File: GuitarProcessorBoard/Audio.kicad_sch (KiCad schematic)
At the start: 33 parts, among them U201 TLV320AIC3204, U202 TL074

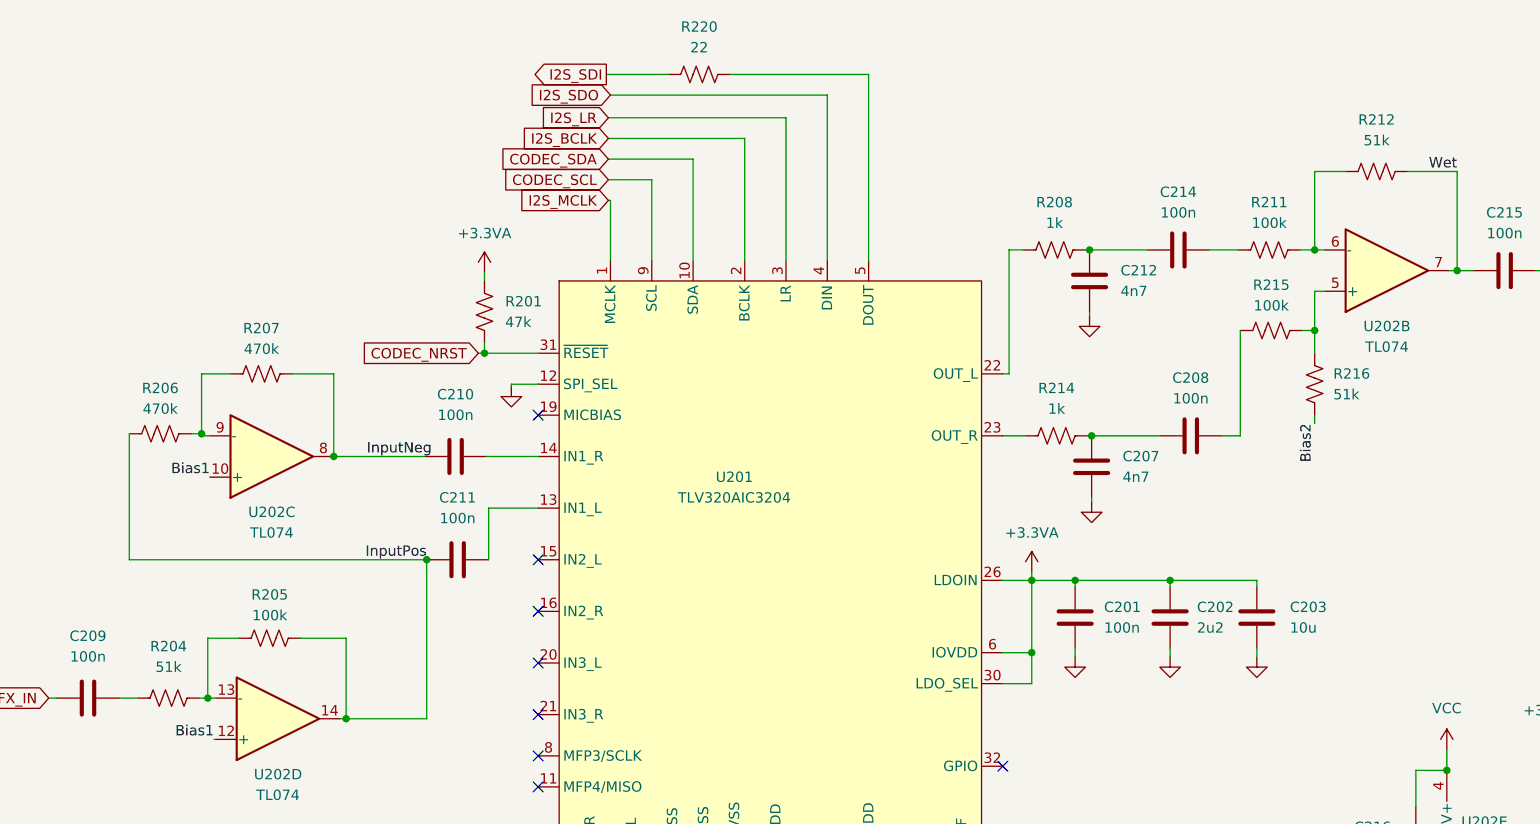
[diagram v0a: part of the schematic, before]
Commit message: tweaked resistor for input/output gain
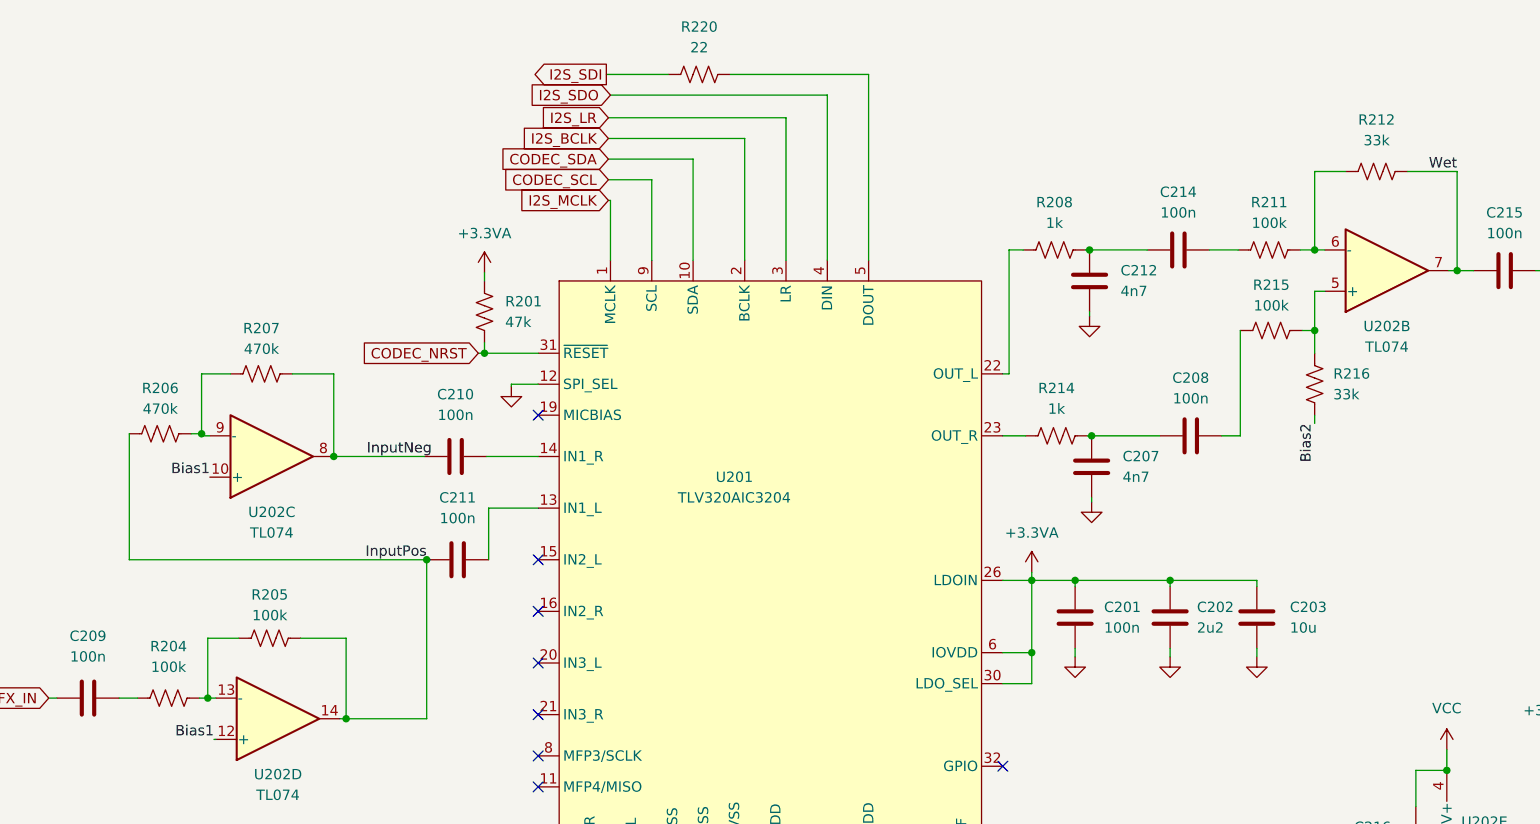
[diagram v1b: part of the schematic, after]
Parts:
- R204: value 51k -> 100k
- R212, R216: value 51k -> 33k
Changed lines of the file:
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@@
 			)
 		)
-		(property "Value" "51k"
+		(property "Value" "100k"
 			(at 38.354 107.95 90)
 			(effects
@@
 			)
 		)
-		(property "Value" "51k"
+		(property "Value" "33k"
 			(at 186.944 43.18 90)
 			(effects
@@
 			)
 		)
-		(property "Value" "51k"
+		(property "Value" "33k"
 			(at 181.61 74.4219 0)
 			(effects

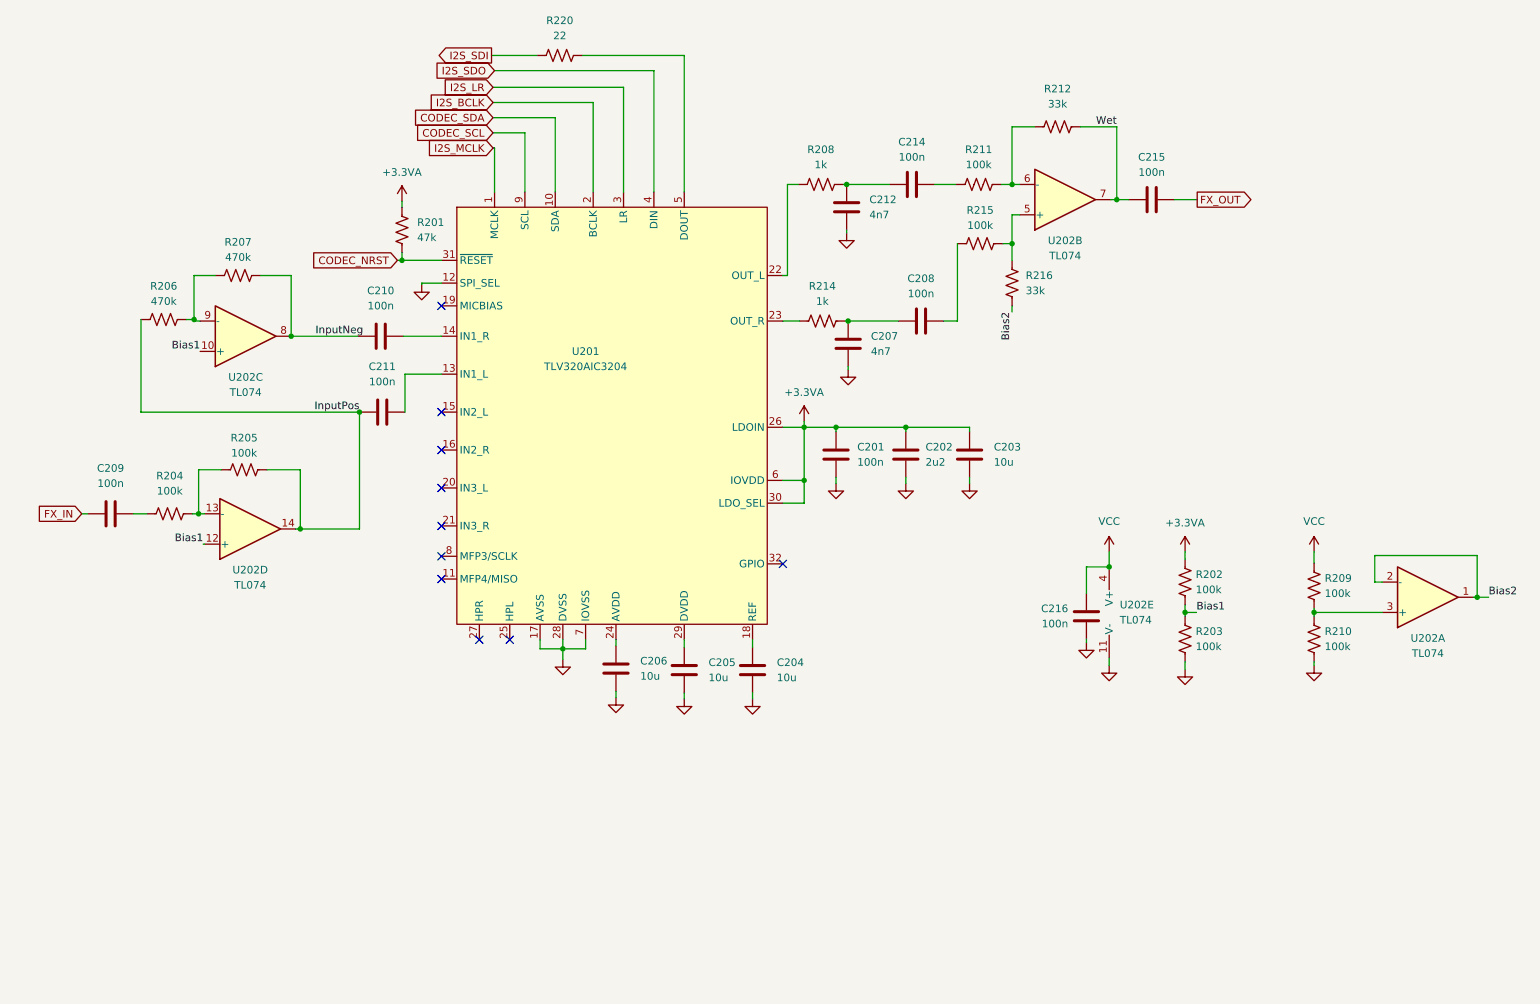
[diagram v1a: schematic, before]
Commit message: updated schematic, re-annotated
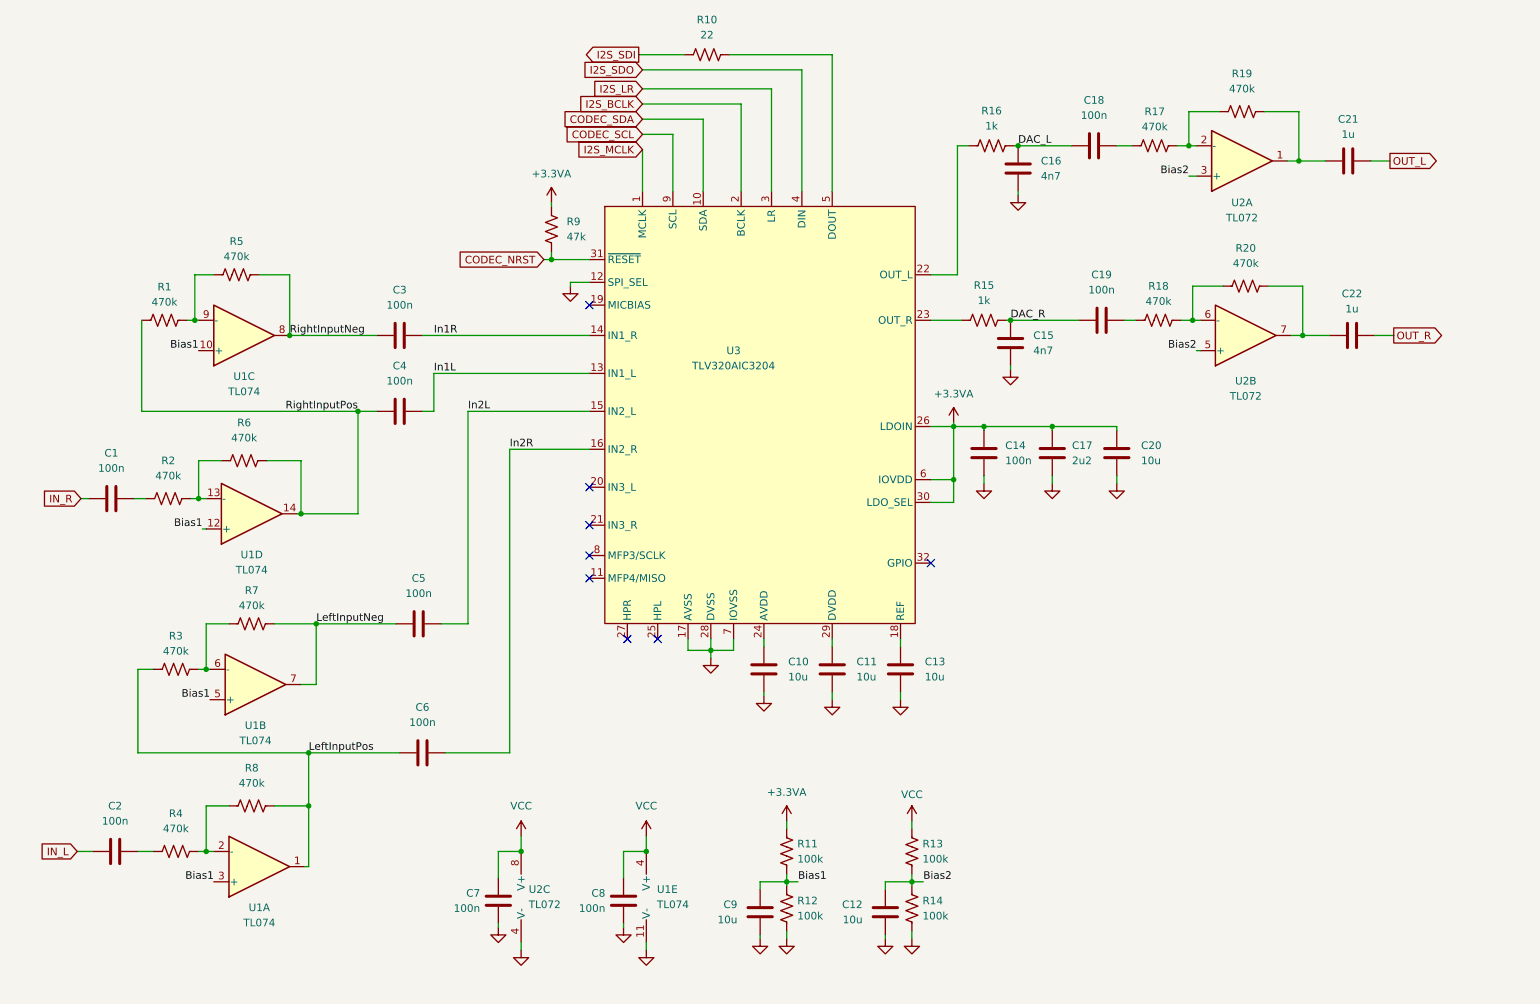
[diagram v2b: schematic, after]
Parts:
- removed C208, C214, C215: 100n, Capacitor_SMD:C_0805_2012Metric, symbol Device:C
- removed R209, R210, R211, R215: 100k, Resistor_SMD:R_0805_2012Metric, symbol Device:R_US
- removed R212, R216: 33k, Resistor_SMD:R_0805_2012Metric, symbol Device:R_US
- added C12, C9: 10u, Capacitor_SMD:C_0805_2012Metric, symbol Device:C
- added C18, C19, C2, C5, C6, C7: 100n, Capacitor_SMD:C_0805_2012Metric, symbol Device:C
- added C21, C22: 1u, Capacitor_SMD:C_0805_2012Metric, symbol Device:C
- added R13, R14: 100k, Resistor_SMD:R_0805_2012Metric, symbol Device:R_US
- added R17, R18, R19, R20, R3, R4, R7, R8: 470k, Resistor_SMD:R_0805_2012Metric, symbol Device:R_US
- added U2: TL072, Package_SO:SOIC-8_3.9x4.9mm_P1.27mm, symbol Amplifier_Operational:TL072
- R2: renamed from R204; value 100k -> 470k
- R6: renamed from R205; value 100k -> 470k
- renumbered C209 to C1, C206 to C10, C205 to C11, C204 to C13, C201 to C14, C207 to C15, C212 to C16, C202 to C17, C203 to C20, C210 to C3, C211 to C4, C216 to C8, R206 to R1, R220 to R10, R202 to R11, R203 to R12, R214 to R15, R208 to R16, R207 to R5, R201 to R9, U202 to U1, U201 to U3
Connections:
- net Bias1: now also U1.3 (+), U1.5 (+), C9.1
- net Bias2: now also C12.1, R13.2, R14.1, U2.3 (+), U2.5 (+); no longer U1.1, U1.2 (-)
- net GND: now also C12.2, C7.2, C9.2, R14.2, U2.4 (V-)
- net VCC: now also C7.1, R13.1, U2.8 (V+)
- net DAC_L: now reaches C16.1, R16.2
- net DAC_L: now also C18.1
- net In1L: now reaches C4.2, U3.13 (IN1_L)
- net In1R: now reaches C3.2, U3.14 (IN1_R)
- net In2L: now reaches U3.15 (IN2_L)
- net In2L: now also C5.2
- net In2R: now reaches U3.16 (IN2_R)
- net In2R: now also C6.2
- net DAC_R: now reaches C15.1, R15.2
- net DAC_R: now also C19.1
- net at U1.6 (-): now also R3.2, R7.1
- net FX_IN renamed IN_R
- net InputNeg renamed RightInputNeg
- net InputPos renamed RightInputPos
- net Wet renamed LeftInputNeg
- net LeftInputNeg: now also C5.1, R7.2
- new net: C22.1, R20.2, U2.7
- new net: R4.2, R8.1, U1.2 (-)
- new net: C2.2, R4.1
- new net: C19.2, R18.1
- new net: R18.2, R20.1, U2.6 (-)
- new net: C21.1, R19.2, U2.1
- new net: R17.2, R19.1, U2.2 (-)
- new net: C18.2, R17.1
- new net IN_L: C2.1
- new net LeftInputPos: C6.1, R3.1, R8.2, U1.1
- new net OUT_L: C21.2
- new net OUT_R: C22.2
- no-connect marks 10 -> 8
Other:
- moved on the sheet: C1, C10, C11, C13, C14, C15, C16, C17, C20, C3, C4, C8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

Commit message: new layout
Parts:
- added TP10: DACR, TestPoint:TestPoint_THTPad_D2.0mm_Drill1.0mm_VAL, symbol Connector:TestPoint
- added TP9: DACL, TestPoint:TestPoint_THTPad_D2.0mm_Drill1.0mm_VAL, symbol Connector:TestPoint
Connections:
- net DAC_L: now also TP9.1
- net DAC_R: now also TP10.1
- net LeftInputNeg: now also U1.8; no longer U1.7
- net LeftInputPos: now also U1.7; no longer U1.1
- net RightInputNeg: now also U1.14; no longer U1.8
- net RightInputPos: now also U1.1; no longer U1.14
- net at R3.2, R7.1: now also U1.9 (-); no longer U1.6 (-)
- net at R1.2, R5.1: now also U1.13 (-); no longer U1.9 (-)
- net at C22.1, R20.2: now also U2.1; no longer U2.7
- net at R4.2, R8.1: now also U1.6 (-); no longer U1.2 (-)
- net at R2.2, R6.1: now also U1.2 (-); no longer U1.13 (-)
- net at R18.2, R20.1: now also U2.2 (-); no longer U2.6 (-)
- net at C21.1, R19.2: now also U2.7; no longer U2.1
- net at R17.2, R19.1: now also U2.6 (-); no longer U2.2 (-)
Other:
- moved on the sheet: U1A, U1B, U1C, U1D, U2A, U2B

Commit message: prelim. routing, DRC passing
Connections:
- net +3.3VA: no longer R9.1
- net LeftInputNeg: now also R7.1; no longer R7.2
- net at R3.2, U1.9 (-): now also R7.2; no longer R7.1
- new net +3.3V: R9.1
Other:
- moved on the sheet: R7
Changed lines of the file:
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@@
 	(symbol
 		(lib_id "Device:R_US")
-		(at 52.07 130.175 90)
-		(unit 1)
-		(body_style 1)
-		(exclude_from_sim no)
-		(in_bom yes)
-		(on_board yes)
-		(in_pos_files yes)
-		(dnp no)
-		(fields_autoplaced yes)
+		(at 52.07 130.175 270)
+		(mirror x)
+		(unit 1)
+		(body_style 1)
+		(exclude_from_sim no)
+		(in_bom yes)
+		(on_board yes)
+		(in_pos_files yes)
+		(dnp no)
 		(property "Reference" "R7"
 			(at 52.07 124.587 90)
@@
 		)
 		(property "Footprint" "Resistor_SMD:R_0805_2012Metric"
-			(at 52.324 129.159 90)
+			(at 51.816 129.159 90)
 			(hide yes)
 			(show_name no)
@@
 				(path "/524c695b-c632-4089-9e9a-ef0f89cad1b2/ef3a9a4a-abe1-4d77-855c-3594c7f88930"
 					(reference "R13")
-					(unit 1)
-				)
-			)
-		)
-	)
-	(symbol
-		(lib_id "power:+3.3VA")
-		(at 102.235 59.69 0)
-		(unit 1)
-		(body_style 1)
-		(exclude_from_sim no)
-		(in_bom yes)
-		(on_board yes)
-		(in_pos_files yes)
-		(dnp no)
-		(fields_autoplaced yes)
-		(property "Reference" "#PWR04"
-			(at 102.235 63.5 0)
-			(hide yes)
-			(show_name no)
-			(do_not_autoplace no)
-			(effects
-				(font
-					(size 1.27 1.27)
-				)
-			)
-		)
-		(property "Value" "+3.3VA"
-			(at 102.235 54.864 0)
-			(show_name no)
-			(do_not_autoplace no)
-			(effects
-				(font
-					(size 1.27 1.27)
-				)
-			)
-		)
-		(property "Footprint" ""
-			(at 102.235 59.69 0)
-			(hide yes)
-			(show_name no)
-			(do_not_autoplace no)
-			(effects
-				(font
-					(size 1.27 1.27)
-				)
-			)
-		)
-		(property "Datasheet" ""
-			(at 102.235 59.69 0)
-			(hide yes)
-			(show_name no)
-			(do_not_autoplace no)
-			(effects
-				(font
-					(size 1.27 1.27)
-				)
-			)
-		)
-		(property "Description" "Power symbol creates a global label with name \"+3.3VA\""
-			(at 102.235 59.69 0)
-			(hide yes)
-			(show_name no)
-			(do_not_autoplace no)
-			(effects
-				(font
-					(size 1.27 1.27)
-				)
-			)
-		)
-		(pin "1"
-		)
-		(instances
-			(project "GuitarProcessorBoard"
-				(path "/524c695b-c632-4089-9e9a-ef0f89cad1b2/ef3a9a4a-abe1-4d77-855c-3594c7f88930"
-					(reference "#PWR04")
 					(unit 1)
 				)
@@
 					(unit 1)
 				)
+			)
+		)
+	)
+	(symbol
+		(lib_id "power:+3.3V")
+		(at 102.235 59.69 0)
+		(unit 1)
+		(body_style 1)
+		(exclude_from_sim no)
+		(in_bom yes)
+		(on_board yes)
+		(in_pos_files yes)
+		(dnp no)
+		(fields_autoplaced yes)
+		(property "Reference" "#PWR04"
+			(at 102.235 63.5 0)
+			(hide yes)
+			(show_name no)
+			(do_not_autoplace no)
+			(effects
+				(font
+					(size 1.27 1.27)
+				)
+			)
+		)
+		(property "Value" "+3.3V"
+			(at 102.235 54.61 0)
+			(show_name no)
+			(do_not_autoplace no)
+			(effects
+				(font
+					(size 1.27 1.27)
+				)
+			)
+		)
+		(property "Footprint" ""
+			(at 102.235 59.69 0)
+			(hide yes)
+			(show_name no)
+			(do_not_autoplace no)
+			(effects
+				(font
+					(size 1.27 1.27)
+				)
+			)
+		)
+		(property "Datasheet" ""
+			(at 102.235 59.69 0)
+			(hide yes)
+			(show_name no)
+			(do_not_autoplace no)
+			(effects
+				(font
+					(size 1.27 1.27)
+				)
+			)
+		)
+		(property "Description" "Power symbol creates a global label with name \"+3.3V\""
+			(at 102.235 59.69 0)
+			(hide yes)
+			(show_name no)
+			(do_not_autoplace no)
+			(effects
+				(font
+					(size 1.27 1.27)
+				)
+			)
+		)
+		(pin "1"
+		)
+		(instances
+			(project "GuitarProcessorBoard"
+				(path "/524c695b-c632-4089-9e9a-ef0f89cad1b2/ef3a9a4a-abe1-4d77-855c-3594c7f88930"
+					(reference "#PWR04")
+					(unit 1)
+				)

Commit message: new layout, pinout switcharoo
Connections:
- net +3.3V is gone; now on net +3.3VA: R9.1
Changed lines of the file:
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@@
-	)
-	(symbol
-		(lib_id "power:+3.3V")
-		(at 102.235 59.69 0)
-		(unit 1)
-		(body_style 1)
-		(exclude_from_sim no)
-		(in_bom yes)
-		(on_board yes)
-		(in_pos_files yes)
-		(dnp no)
-		(fields_autoplaced yes)
-		(property "Reference" "#PWR04"
-			(at 102.235 63.5 0)
-			(hide yes)
-			(show_name no)
-			(do_not_autoplace no)
-			(effects
-				(font
-					(size 1.27 1.27)
-				)
-			)
-		)
-		(property "Value" "+3.3V"
-			(at 102.235 54.61 0)
-			(show_name no)
-			(do_not_autoplace no)
-			(effects
-				(font
-					(size 1.27 1.27)
-				)
-			)
-		)
-		(property "Footprint" ""
-			(at 102.235 59.69 0)
-			(hide yes)
-			(show_name no)
-			(do_not_autoplace no)
-			(effects
-				(font
-					(size 1.27 1.27)
-				)
-			)
-		)
-		(property "Datasheet" ""
-			(at 102.235 59.69 0)
-			(hide yes)
-			(show_name no)
-			(do_not_autoplace no)
-			(effects
-				(font
-					(size 1.27 1.27)
-				)
-			)
-		)
-		(property "Description" "Power symbol creates a global label with name \"+3.3V\""
-			(at 102.235 59.69 0)
-			(hide yes)
-			(show_name no)
-			(do_not_autoplace no)
-			(effects
-				(font
-					(size 1.27 1.27)
-				)
-			)
-		)
-		(pin "1"
-		)
-		(instances
-			(project "GuitarProcessorBoard"
-				(path "/524c695b-c632-4089-9e9a-ef0f89cad1b2/ef3a9a4a-abe1-4d77-855c-3594c7f88930"
-					(reference "#PWR04")
-					(unit 1)
-				)
-			)
-		)
 	)
 	(symbol
@@
 					(unit 1)
 				)
+			)
+		)
+	)
+	(symbol
+		(lib_id "power:+3.3VA")
+		(at 102.235 59.69 0)
+		(unit 1)
+		(body_style 1)
+		(exclude_from_sim no)
+		(in_bom yes)
+		(on_board yes)
+		(in_pos_files yes)
+		(dnp no)
+		(fields_autoplaced yes)
+		(property "Reference" "#PWR027"
+			(at 102.235 63.5 0)
+			(hide yes)
+			(show_name no)
+			(do_not_autoplace no)
+			(effects
+				(font
+					(size 1.27 1.27)
+				)
+			)
+		)
+		(property "Value" "+3.3VA"
+			(at 102.235 54.864 0)
+			(show_name no)
+			(do_not_autoplace no)
+			(effects
+				(font
+					(size 1.27 1.27)
+				)
+			)
+		)
+		(property "Footprint" ""
+			(at 102.235 59.69 0)
+			(hide yes)
+			(show_name no)
+			(do_not_autoplace no)
+			(effects
+				(font
+					(size 1.27 1.27)
+				)
+			)
+		)
+		(property "Datasheet" ""
+			(at 102.235 59.69 0)
+			(hide yes)
+			(show_name no)
+			(do_not_autoplace no)
+			(effects
+				(font
+					(size 1.27 1.27)
+				)
+			)
+		)
+		(property "Description" "Power symbol creates a global label with name \"+3.3VA\""
+			(at 102.235 59.69 0)
+			(hide yes)
+			(show_name no)
+			(do_not_autoplace no)
+			(effects
+				(font
+					(size 1.27 1.27)
+				)
+			)
+		)
+		(pin "1"
+		)
+		(instances
+			(project "GuitarProcessorBoard"
+				(path "/524c695b-c632-4089-9e9a-ef0f89cad1b2/ef3a9a4a-abe1-4d77-855c-3594c7f88930"
+					(reference "#PWR027")
+					(unit 1)
+				)
